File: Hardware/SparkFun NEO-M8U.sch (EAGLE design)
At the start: 50 parts, among them J13 U.FL, J2 Qwiic Right Angle, J4 Qwiic Right Angle, U1 U-BLOX_NEO-M8T, U2 3.3V

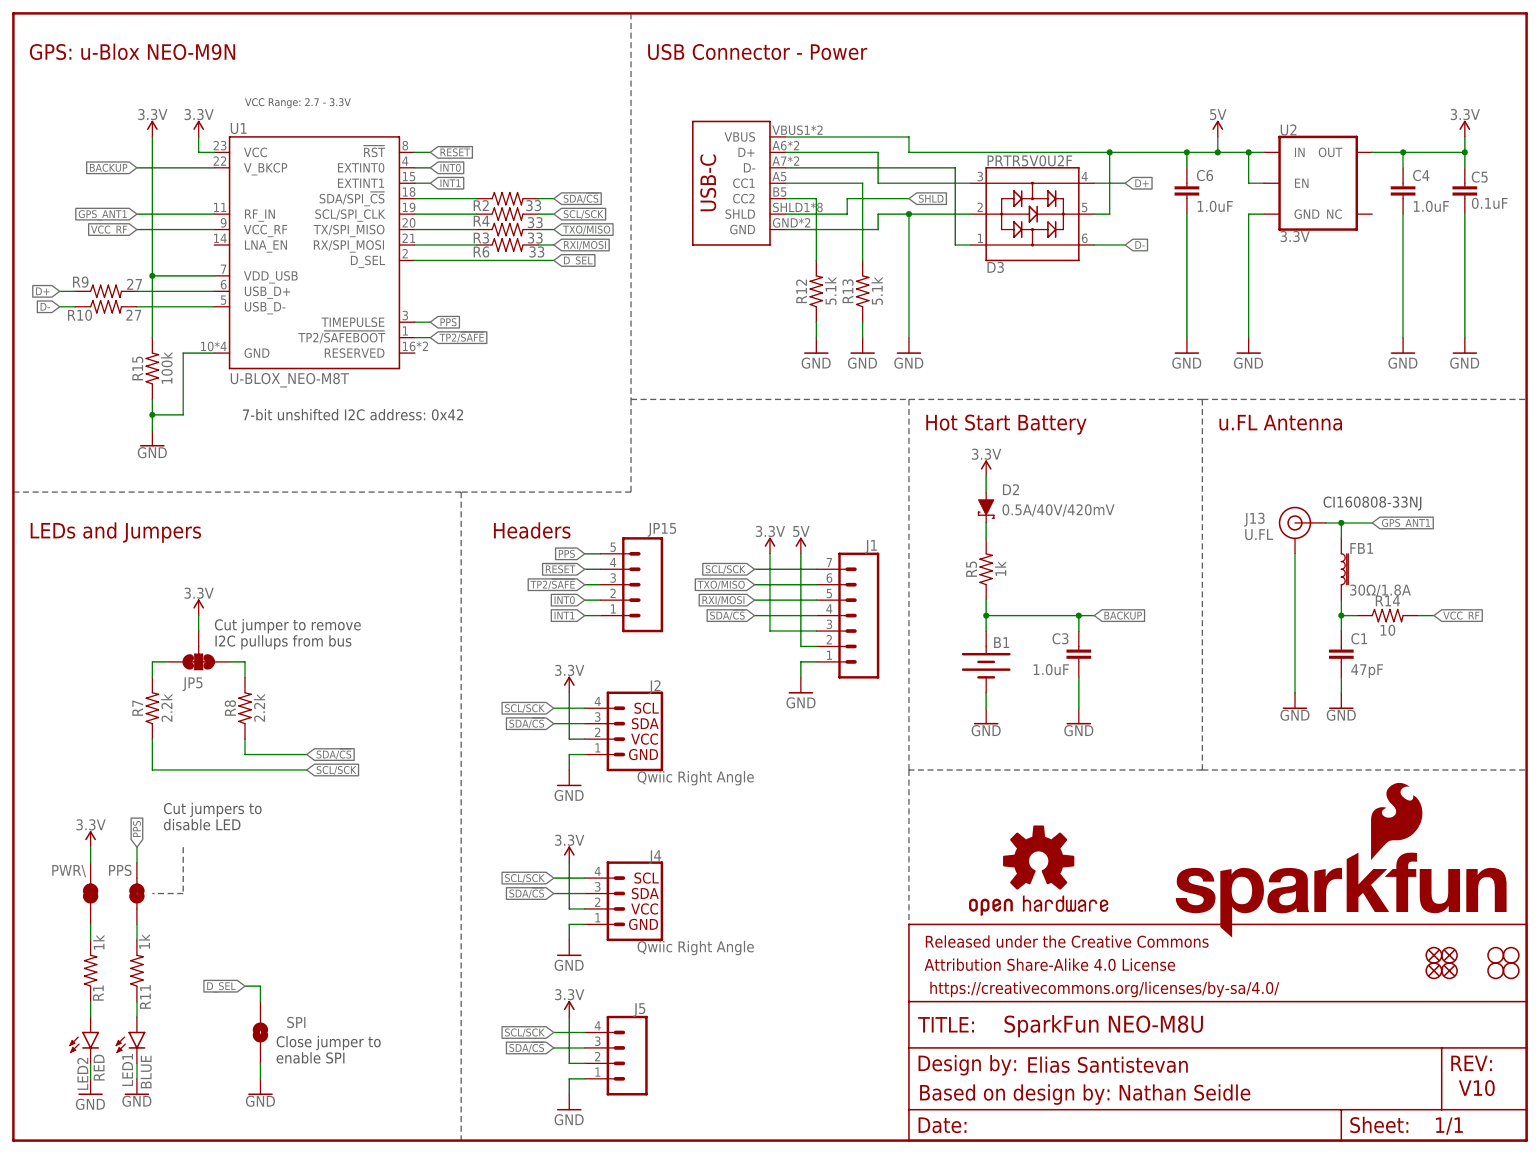
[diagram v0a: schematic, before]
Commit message: Updates design with the M8U module
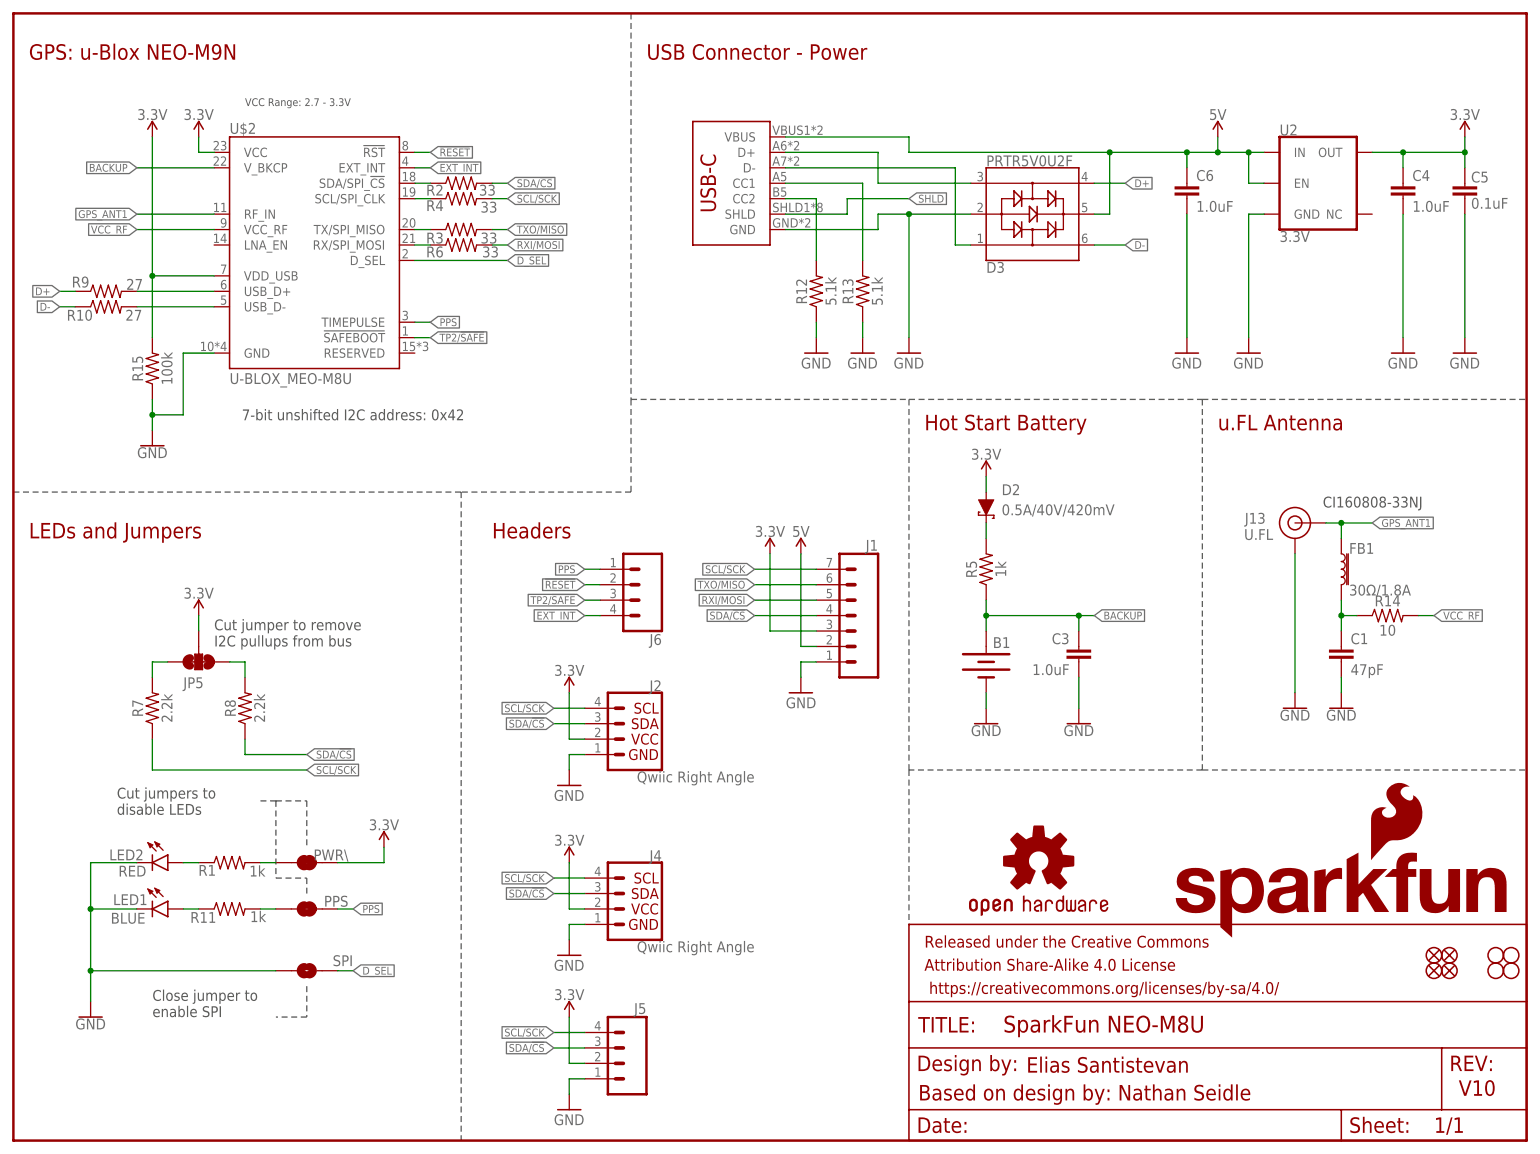
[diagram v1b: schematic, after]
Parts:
- removed JP15: (no value), SparkFun-Connectors:CONN_05NO_SILK
- removed U1: U-BLOX_NEO-M8T, SparkFun-GPS:U-BLOX_NEO-M8T
- added J6: (no value), SparkFun-Connectors:CONN_041X04_NO_SILK
- added U$2: U-BLOX_MEO-M8U, SparkFun-GPS:U-BLOX_MEO-M8U
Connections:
- removed net INT0: JP15.2, U1.EXTINT0
- removed net INT1: JP15.1, U1.EXTINT1
- removed net RXLV: R6.1, U1.RX/SPI_MOSI
- removed net TXLV: R3.1, U1.TX/SPI_MISO
- new net EXT_INT: J6.4, U$2.EXT_INT
- new net N$15: R3.1, U$2.TX/SPI_MISO
- new net N$16: R6.1, U$2.RX/SPI_MOSI
- net !RESET: now also J6.2, U$2.!RST; no longer JP15.4, U1.!RST
- net 3.3V: now also U$2.VCC, U$2.VDD_USB; no longer U1.VCC, U1.VDD_USB
- net BACKUP: now also U$2.V_BKCP; no longer U1.V_BKCP
- net D_SEL: now also U$2.D_SEL; no longer U1.D_SEL
- net GND: now also U$2.GND; no longer U1.GND
- net GPS_ANT1: now also U$2.RF_IN; no longer U1.RF_IN
- net N$11: now also U$2.USB_D+; no longer U1.USB_D+
- net N$12: now also U$2.USB_D-; no longer U1.USB_D-
- net N$13: now also U$2.SCL/SPI_CLK; no longer U1.SCL/SPI_CLK
- net N$3: now also U$2.SDA/SPI_!CS!; no longer U1.SDA/SPI_!CS!
- net PPS: now also J6.1, U$2.TIMEPULSE; no longer JP15.5, U1.TIMEPULSE
- net TP2/!SAFE: now also J6.3, U$2.!SAFEBOOT!; no longer JP15.3, U1.TP2/!SAFEBOOT!
- net VCC_RF: now also U$2.VCC_RF; no longer U1.VCC_RF
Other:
- note added: "Cut jumpers to disable LEDs"
- note removed: "Cut jumpers to disable LED"
- moved on the sheet: LED1, LED2, PPS, PWR\, R1, R11, R2, R3, R4, R6, SPI

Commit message: Updates the ground and shield pour
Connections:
- net SHLD renamed SHIELD
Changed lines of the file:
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@@
 <class number="2" name="3.3V" width="0.508" drill="0">
+</class>
+<class number="3" name="USB-C" width="0" drill="0">
 </class>
 </classes>
@@
 <part name="R7" library="SparkFun-Resistors" deviceset="2.2KOHM" device="-0603-1/10W-1%" value="2.2k"/>
 <part name="R8" library="SparkFun-Resistors" deviceset="2.2KOHM" device="-0603-1/10W-1%" value="2.2k"/>
-<part name="JP5" library="SparkFun-Jumpers" deviceset="JUMPER-SMT_3_2-NC_TRACE" device="_SILK" value="JUMPER-SMT_3_2-NC_TRACE_SILK"/>
+<part name="JP5" library="SparkFun-Jumpers" deviceset="JUMPER-SMT_3_2-NC_TRACE" device="_SILK" package3d_urn="urn:adsk.eagle:package:39289/1" value="JUMPER-SMT_3_2-NC_TRACE_SILK"/>
 <part name="SUPPLY9" library="SparkFun-PowerSymbols" deviceset="3.3V" device=""/>
 <part name="LED1" library="SparkFun-LED" deviceset="LED-BLUE" device="0603" value="BLUE"/>
-<part name="PPS" library="SparkFun-Jumpers" deviceset="JUMPER-SMT_2_NC_TRACE" device="_SILK" value="JUMPER-SMT_2_NC_TRACE_SILK"/>
+<part name="PPS" library="SparkFun-Jumpers" deviceset="JUMPER-SMT_2_NC_TRACE" device="_SILK" package3d_urn="urn:adsk.eagle:package:39281/1" value="JUMPER-SMT_2_NC_TRACE_SILK"/>
 <part name="D2" library="SparkFun-DiscreteSemi" deviceset="DIODE-SCHOTTKY" device="-PMEG4005EJ" value="0.5A/40V/420mV"/>
 <part name="SUPPLY5" library="SparkFun-PowerSymbols" deviceset="3.3V" device=""/>
@@
 <part name="R9" library="SparkFun-Resistors" deviceset="27OHM" device="-0603-1/10W-1%" value="27"/>
 <part name="R10" library="SparkFun-Resistors" deviceset="27OHM" device="-0603-1/10W-1%" value="27"/>
-<part name="SPI" library="SparkFun-Jumpers" deviceset="JUMPER-SMT_2_NO" device="_SILK" value="JUMPER-SMT_2_NO_SILK"/>
+<part name="SPI" library="SparkFun-Jumpers" deviceset="JUMPER-SMT_2_NO" device="_SILK" package3d_urn="urn:adsk.eagle:package:39279/1" value="JUMPER-SMT_2_NO_SILK"/>
 <part name="GND2" library="SparkFun-PowerSymbols" deviceset="GND" device=""/>
 <part name="C1" library="SparkFun-Capacitors" deviceset="47PF" device="-0603-50V-5%" value="47pF"/>
@@
 <part name="SUPPLY11" library="SparkFun-PowerSymbols" deviceset="5V" device=""/>
 <part name="LOGO2" library="SparkFun-Aesthetics" deviceset="SFE_LOGO_NAME_FLAME" device=".1_INCH"/>
-<part name="PWR\" library="SparkFun-Jumpers" deviceset="JUMPER-SMT_2_NC_TRACE" device="_SILK" value="JUMPER-SMT_2_NC_TRACE_SILK"/>
+<part name="PWR\" library="SparkFun-Jumpers" deviceset="JUMPER-SMT_2_NC_TRACE" device="_SILK" package3d_urn="urn:adsk.eagle:package:39281/1" value="JUMPER-SMT_2_NC_TRACE_SILK"/>
 <part name="D3" library="SparkFun-IC-Power" deviceset="PRTR5V0U2" device="F"/>
 <part name="J5" library="SparkFun-Connectors" deviceset="CONN_04" device="1X04_NO_SILK"/>
@@
 </segment>
 </net>
-<net name="SHLD" class="0">
-<segment>
-<wire x1="137.16" y1="154.94" x2="147.32" y2="154.94" width="0.1524" layer="91"/>
-<label x="147.32" y="154.94" size="1.27" layer="95" font="vector" xref="yes"/>
-<pinref part="J3" gate="J1" pin="SHLD"/>
-<wire x1="127" y1="152.4" x2="137.16" y2="152.4" width="0.1524" layer="91"/>
-<wire x1="137.16" y1="152.4" x2="137.16" y2="154.94" width="0.1524" layer="91"/>
-</segment>
-</net>
 <net name="USB_D-" class="0">
 <segment>
@@
 </segment>
 </net>
+<net name="SHIELD" class="0">
+<segment>
+<pinref part="J3" gate="J1" pin="SHLD"/>
+<wire x1="127" y1="152.4" x2="137.16" y2="152.4" width="0.1524" layer="91"/>
+<wire x1="137.16" y1="152.4" x2="137.16" y2="154.94" width="0.1524" layer="91"/>
+<wire x1="137.16" y1="154.94" x2="142.24" y2="154.94" width="0.1524" layer="91"/>
+<label x="142.24" y="154.94" size="1.27" layer="95" xref="yes"/>
+</segment>
+</net>
 </nets>
 </sheet>
@@
 which will not be processed correctly with this version.
 </note>
+<note version="8.3" severity="warning">
+Since Version 8.3, EAGLE supports URNs for individual library
+assets (packages, symbols, and devices). The URNs of those assets
+will not be understood (or retained) with this version.
+</note>
+<note version="8.3" severity="warning">
+Since Version 8.3, EAGLE supports the association of 3D packages
+with devices in libraries, schematics, and board files. Those 3D
+packages will not be understood (or retained) with this version.
+</note>
 </compatibility>

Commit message: Updates design to improve ground pout
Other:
- note added: "V01"
- note removed: "V10"
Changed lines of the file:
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@@
 <sheet>
 <plain>
-<text x="237.744" y="7.366" size="2.54" layer="94" font="vector">V10</text>
+<text x="237.744" y="7.366" size="2.54" layer="94" font="vector">V01</text>
 <text x="55.88" y="119.38" size="1.778" layer="97" font="vector" align="center">7-bit unshifted I2C address: 0x42</text>
 <wire x1="0" y1="106.68" x2="73.66" y2="106.68" width="0.1524" layer="97" style="shortdash"/>
